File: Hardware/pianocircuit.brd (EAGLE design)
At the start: 160 x 82.2 mm, 64 parts, among them IC1 LM386M-1

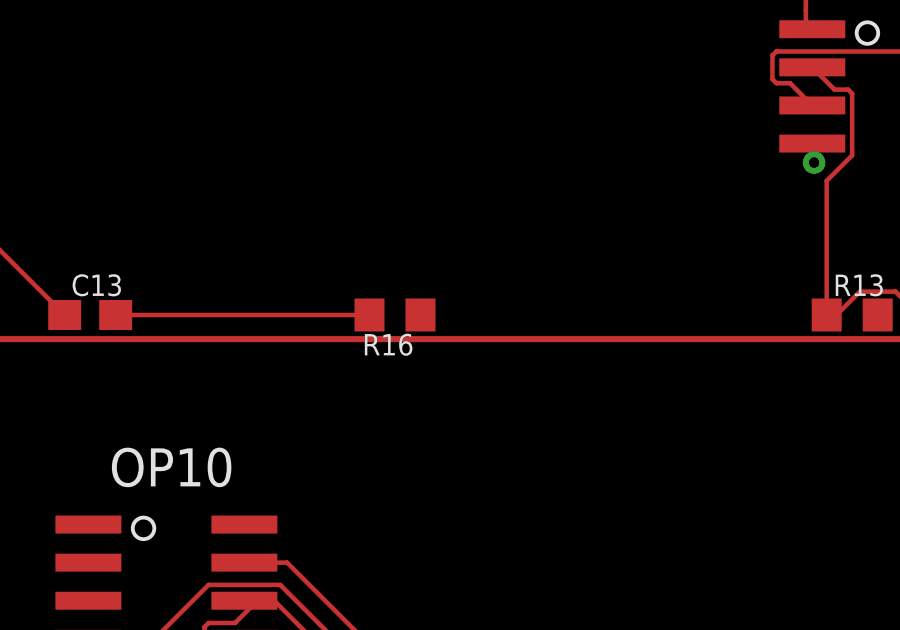
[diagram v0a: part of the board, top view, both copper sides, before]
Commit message: Routed Board and Updated Schematic
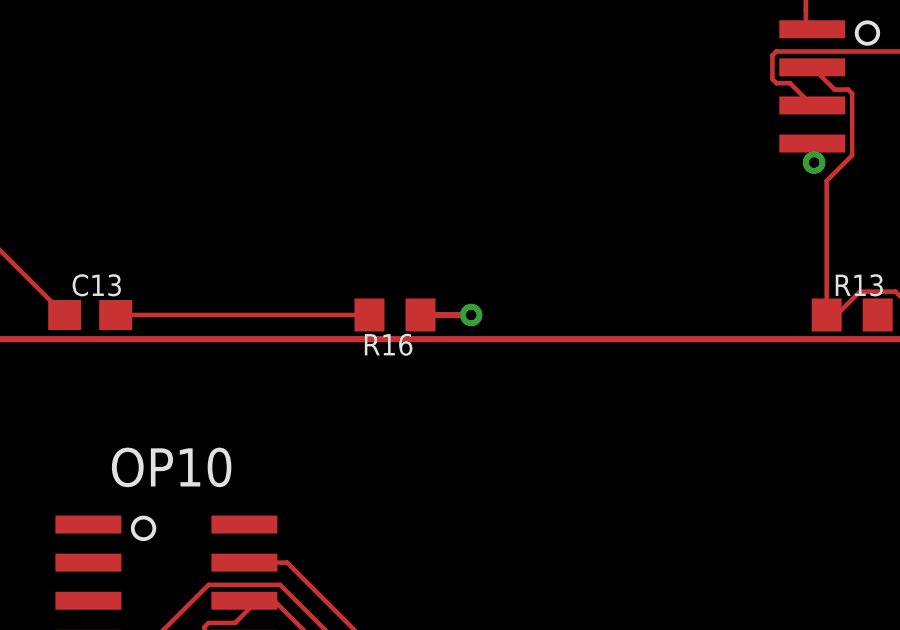
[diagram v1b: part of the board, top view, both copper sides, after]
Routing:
- net GND: track 28.0 -> 29.7 mm, vias 21 -> 22
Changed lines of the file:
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@@
 <wire x1="137.16" y1="38.735" x2="137.16" y2="38.1" width="0.2032" layer="1"/>
 <via x="137.16" y="38.1" extent="1-16" drill="0.35"/>
+<wire x1="38.95" y1="33.02" x2="40.64" y2="33.02" width="0.2032" layer="1"/>
+<via x="40.64" y="33.02" extent="1-16" drill="0.35"/>
 <wire x1="156.63" y1="16.51" x2="157.06" y2="19.05" width="0" layer="19" extent="1-1"/>
 <wire x1="154.94" y1="7.62" x2="156.63" y2="16.51" width="0" layer="19" extent="1-1"/>
-<wire x1="38.95" y1="33.02" x2="52.07" y2="38.1" width="0" layer="19" extent="1-1"/>
+<wire x1="138.43" y1="10.16" x2="153.25" y2="7.62" width="0" layer="19" extent="1-1"/>
+<wire x1="132.084075" y1="6.345925" x2="138.43" y2="10.16" width="0" layer="19" extent="1-1"/>
+<wire x1="123.61" y1="33.02" x2="138.37" y2="10.795" width="0" layer="19" extent="1-1"/>
+<wire x1="118.96" y1="33.02" x2="123.02256875" y2="34.12256875" width="0" layer="19" extent="1-1"/>
+<wire x1="106.68" y1="38.1" x2="118.96" y2="33.02" width="0" layer="19" extent="1-1"/>
+<wire x1="137.16" y1="38.1" x2="123.61" y2="33.02" width="0" layer="19" extent="1-1"/>
+<wire x1="107.95" y1="17.78" x2="119.38" y2="31.75" width="0" layer="19" extent="1-1"/>
+<wire x1="91.44" y1="12.7" x2="106.26" y2="17.78" width="0" layer="19" extent="1-1"/>
+<wire x1="83.82" y1="11.43" x2="91.44" y2="12.7" width="0" layer="19" extent="1-1"/>
+<wire x1="78.74" y1="13.12" x2="83.76" y2="12.065" width="0" layer="19" extent="1-1"/>
+<wire x1="64.77" y1="33.02" x2="77.47" y2="12.7" width="0" layer="19" extent="1-1"/>
+<wire x1="52.07" y1="38.1" x2="63.08" y2="33.02" width="0" layer="19" extent="1-1"/>
+<wire x1="40.64" y1="33.02" x2="52.07" y2="38.1" width="0" layer="19" extent="1-1"/>
+<wire x1="77.47" y1="38.1" x2="64.77" y2="33.02" width="0" layer="19" extent="1-1"/>
+<wire x1="27.88" y1="22.225" x2="38.95" y2="33.02" width="0" layer="19" extent="1-1"/>
+<wire x1="19.05" y1="15.24" x2="27.94" y2="21.59" width="0" layer="19" extent="1-1"/>
+<wire x1="16.51" y1="11.43" x2="19.47" y2="13.97" width="0" layer="19" extent="1-1"/>
+<wire x1="12.7" y1="6.35" x2="16.09" y2="10.16" width="0" layer="19" extent="1-1"/>
+<wire x1="20.32" y1="33.02" x2="27.88" y2="22.225" width="0" layer="19" extent="1-1"/>
+<wire x1="17.78" y1="54.61" x2="18.63" y2="33.02" width="0" layer="19" extent="1-1"/>
+<wire x1="16.57" y1="56.515" x2="16.57" y2="55.245" width="0" layer="19" extent="1-1"/>
 <wire x1="2.54" y1="52.07" x2="16.57" y2="55.245" width="0" layer="19" extent="1-1"/>
 </signal>

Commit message: Fixed Routing Errors
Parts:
- added R4: 3.3M, LinnesLab-Passives:R0603
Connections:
- new net N$12: R4.2
- net N$60: now also R4.1
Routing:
- net N$10: track 39.0 -> 91.5 mm
- net GND: track 29.7 -> 44.0 mm, vias 22 -> 24
- net N$60: track 14.3 -> 20.6 mm
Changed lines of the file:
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@@
 <attribute name="VALUE" x="4.52" y="64.625" size="1.27" layer="27"/>
+</element>
+<element name="R4" library="LinnesLab-Passives" package="R0603" package3d_urn="urn:adsk.eagle:package:15661944/2" value="3.3M" x="35.56" y="15.24" smashed="yes">
+<attribute name="NAME" x="34.925" y="15.875" size="0.7112" layer="25"/>
+<attribute name="VALUE" x="34.925" y="13.335" size="0.7112" layer="27"/>
 </element>
 </elements>
@@
 <wire x1="19.05" y1="13.97" x2="19.05" y2="15.24" width="0.2032" layer="1"/>
 <via x="19.05" y="15.24" extent="1-16" drill="0.35"/>
-<wire x1="16.57" y1="55.245" x2="17.78" y2="55.245" width="0.2032" layer="1"/>
-<wire x1="17.78" y1="55.245" x2="17.78" y2="54.8056" width="0.2032" layer="1"/>
-<wire x1="17.78" y1="54.8056" x2="17.78" y2="54.61" width="0.2032" layer="1"/>
-<via x="17.78" y="54.8056" extent="1-16" drill="0.35"/>
-<wire x1="16.57" y1="56.515" x2="16.57" y2="57.15" width="0.2032" layer="1"/>
-<wire x1="16.57" y1="57.15" x2="16.51" y2="57.15" width="0.2032" layer="1"/>
-<via x="16.51" y="57.15" extent="1-16" drill="0.35"/>
+<wire x1="16.57" y1="55.245" x2="19.05" y2="55.245" width="0.2032" layer="1"/>
+<wire x1="19.05" y1="55.245" x2="19.05" y2="54.8056" width="0.2032" layer="1"/>
+<wire x1="19.05" y1="54.8056" x2="19.05" y2="54.61" width="0.2032" layer="1"/>
+<via x="19.05" y="54.8056" extent="1-16" drill="0.35"/>
+<wire x1="16.57" y1="56.515" x2="16.57" y2="58.42" width="0.2032" layer="1"/>
+<wire x1="16.57" y1="58.42" x2="16.51" y2="58.42" width="0.2032" layer="1"/>
+<via x="16.51" y="58.42" extent="1-16" drill="0.35"/>
 <wire x1="18.63" y1="33.02" x2="20.32" y2="33.02" width="0.2032" layer="1"/>
 <via x="20.32" y="33.02" extent="1-16" drill="0.35"/>
@@
 <wire x1="91.44" y1="11.43" x2="91.44" y2="12.7" width="0.2032" layer="1"/>
 <via x="91.44" y="12.7" extent="1-16" drill="0.35"/>
-<wire x1="83.76" y1="12.065" x2="83.76" y2="11.43" width="0.2032" layer="1"/>
-<wire x1="83.76" y1="11.43" x2="83.82" y2="11.43" width="0.2032" layer="1"/>
-<via x="83.82" y="11.43" extent="1-16" drill="0.35"/>
+<wire x1="83.76" y1="12.065" x2="83.76" y2="10.16" width="0.2032" layer="1"/>
+<wire x1="83.76" y1="10.16" x2="83.82" y2="10.16" width="0.2032" layer="1"/>
+<via x="83.82" y="10.16" extent="1-16" drill="0.35"/>
 <wire x1="153.25" y1="7.62" x2="154.94" y2="7.62" width="0.2032" layer="1"/>
 <via x="154.94" y="7.62" extent="1-16" drill="0.35"/>
@@
 <contactref element="OP1" pad="4"/>
 <contactref element="OP10" pad="4"/>
-<wire x1="52.01" y1="38.735" x2="52.07" y2="38.735" width="0.2032" layer="1"/>
-<wire x1="52.07" y1="38.735" x2="52.07" y2="38.1" width="0.2032" layer="1"/>
-<via x="52.07" y="38.1" extent="1-16" drill="0.35"/>
+<wire x1="52.01" y1="38.735" x2="51.375" y2="38.1" width="0.2032" layer="1"/>
+<wire x1="51.375" y1="38.1" x2="49.53" y2="38.1" width="0.2032" layer="1"/>
+<via x="49.53" y="38.1" extent="1-16" drill="0.35"/>
 <wire x1="77.41" y1="38.735" x2="77.47" y2="38.735" width="0.2032" layer="1"/>
-<wire x1="77.47" y1="38.735" x2="77.47" y2="38.1" width="0.2032" layer="1"/>
-<via x="77.47" y="38.1" extent="1-16" drill="0.35"/>
+<wire x1="77.47" y1="38.735" x2="77.47" y2="36.83" width="0.2032" layer="1"/>
+<via x="77.47" y="36.83" extent="1-16" drill="0.35"/>
 <wire x1="27.88" y1="22.225" x2="27.94" y2="22.225" width="0.2032" layer="1"/>
 <wire x1="27.94" y1="22.225" x2="27.94" y2="21.59" width="0.2032" layer="1"/>
 <via x="27.94" y="21.59" extent="1-16" drill="0.35"/>
 <wire x1="106.62" y1="38.735" x2="106.68" y2="38.735" width="0.2032" layer="1"/>
-<wire x1="106.68" y1="38.735" x2="106.68" y2="38.1" width="0.2032" layer="1"/>
-<via x="106.68" y="38.1" extent="1-16" drill="0.35"/>
+<wire x1="106.68" y1="38.735" x2="106.68" y2="36.83" width="0.2032" layer="1"/>
+<via x="106.68" y="36.83" extent="1-16" drill="0.35"/>
 <wire x1="138.37" y1="10.795" x2="138.43" y2="10.795" width="0.2032" layer="1"/>
-<wire x1="138.43" y1="10.795" x2="138.43" y2="10.16" width="0.2032" layer="1"/>
-<via x="138.43" y="10.16" extent="1-16" drill="0.35"/>
+<wire x1="138.43" y1="10.795" x2="138.43" y2="8.89" width="0.2032" layer="1"/>
+<via x="138.43" y="8.89" extent="1-16" drill="0.35"/>
 <wire x1="137.1" y1="38.735" x2="137.16" y2="38.735" width="0.2032" layer="1"/>
-<wire x1="137.16" y1="38.735" x2="137.16" y2="38.1" width="0.2032" layer="1"/>
-<via x="137.16" y="38.1" extent="1-16" drill="0.35"/>
+<wire x1="137.16" y1="38.735" x2="137.16" y2="36.83" width="0.2032" layer="1"/>
+<via x="137.16" y="36.83" extent="1-16" drill="0.35"/>
 <wire x1="38.95" y1="33.02" x2="40.64" y2="33.02" width="0.2032" layer="1"/>
 <via x="40.64" y="33.02" extent="1-16" drill="0.35"/>
-<wire x1="156.63" y1="16.51" x2="157.06" y2="19.05" width="0" layer="19" extent="1-1"/>
-<wire x1="154.94" y1="7.62" x2="156.63" y2="16.51" width="0" layer="19" extent="1-1"/>
-<wire x1="138.43" y1="10.16" x2="153.25" y2="7.62" width="0" layer="19" extent="1-1"/>
-<wire x1="132.084075" y1="6.345925" x2="138.43" y2="10.16" width="0" layer="19" extent="1-1"/>
-<wire x1="123.61" y1="33.02" x2="138.37" y2="10.795" width="0" layer="19" extent="1-1"/>
-<wire x1="118.96" y1="33.02" x2="123.02256875" y2="34.12256875" width="0" layer="19" extent="1-1"/>
-<wire x1="106.68" y1="38.1" x2="118.96" y2="33.02" width="0" layer="19" extent="1-1"/>
-<wire x1="137.16" y1="38.1" x2="123.61" y2="33.02" width="0" layer="19" extent="1-1"/>
-<wire x1="107.95" y1="17.78" x2="119.38" y2="31.75" width="0" layer="19" extent="1-1"/>
-<wire x1="91.44" y1="12.7" x2="106.26" y2="17.78" width="0" layer="19" extent="1-1"/>
-<wire x1="83.82" y1="11.43" x2="91.44" y2="12.7" width="0" layer="19" extent="1-1"/>
-<wire x1="78.74" y1="13.12" x2="83.76" y2="12.065" width="0" layer="19" extent="1-1"/>
-<wire x1="64.77" y1="33.02" x2="77.47" y2="12.7" width="0" layer="19" extent="1-1"/>
-<wire x1="52.07" y1="38.1" x2="63.08" y2="33.02" width="0" layer="19" extent="1-1"/>
-<wire x1="40.64" y1="33.02" x2="52.07" y2="38.1" width="0" layer="19" extent="1-1"/>
-<wire x1="77.47" y1="38.1" x2="64.77" y2="33.02" width="0" layer="19" extent="1-1"/>
-<wire x1="27.88" y1="22.225" x2="38.95" y2="33.02" width="0" layer="19" extent="1-1"/>
-<wire x1="19.05" y1="15.24" x2="27.94" y2="21.59" width="0" layer="19" extent="1-1"/>
-<wire x1="16.51" y1="11.43" x2="19.47" y2="13.97" width="0" layer="19" extent="1-1"/>
-<wire x1="12.7" y1="6.35" x2="16.09" y2="10.16" width="0" layer="19" extent="1-1"/>
-<wire x1="20.32" y1="33.02" x2="27.88" y2="22.225" width="0" layer="19" extent="1-1"/>
-<wire x1="17.78" y1="54.61" x2="18.63" y2="33.02" width="0" layer="19" extent="1-1"/>
-<wire x1="16.57" y1="56.515" x2="16.57" y2="55.245" width="0" layer="19" extent="1-1"/>
-<wire x1="2.54" y1="52.07" x2="16.57" y2="55.245" width="0" layer="19" extent="1-1"/>
+<wire x1="156.63" y1="16.51" x2="154.94" y2="16.51" width="0.1524" layer="1"/>
+<via x="154.94" y="16.51" extent="1-16" drill="0.35"/>
+<wire x1="157.06" y1="19.05" x2="157.06" y2="19.47" width="0.1524" layer="1"/>
+<wire x1="157.06" y1="19.47" x2="156.21" y2="20.32" width="0.1524" layer="1"/>
+<via x="156.21" y="20.32" extent="1-16" drill="0.35"/>
+<wire x1="16.57" y1="55.245" x2="2.54" y2="52.07" width="0" layer="19" extent="1-1"/>
 </signal>
 <signal name="N$2">
@@
 <wire x1="134.62" y1="39.37" x2="135.255" y2="40.005" width="0.1524" layer="1"/>
 <wire x1="135.255" y1="40.005" x2="137.1" y2="40.005" width="0.1524" layer="1"/>
-<wire x1="129.96" y1="5.08" x2="158.33" y2="5.08" width="0" layer="19" extent="1-1"/>
+<wire x1="140.7146875" y1="18.5586" x2="139.5253125" y2="18.5586" width="0.1524" layer="1"/>
+<wire x1="139.5253125" y1="18.5586" x2="139.3914" y2="18.4246875" width="0.1524" layer="1"/>
+<wire x1="139.3914" y1="18.4246875" x2="139.3914" y2="17.1353125" width="0.1524" layer="1"/>
+<wire x1="158.33" y1="5.08" x2="158.0032875" y2="5.08" width="0.1524" layer="1"/>
+<wire x1="158.0032875" y1="5.08" x2="157.2246875" y2="4.3014" width="0.1524" layer="1"/>
+<wire x1="139.3914" y1="17.1353125" x2="139.6986" y2="16.8281125" width="0.1524" layer="1"/>
+<wire x1="139.6986" y1="16.8281125" x2="139.6986" y2="9.30045" width="0.1524" layer="1"/>
+<wire x1="139.6986" y1="9.30045" x2="138.32295" y2="7.9248" width="0.1524" layer="1"/>
+<wire x1="140.8986" y1="18.3746875" x2="140.7146875" y2="18.5586" width="0.1524" layer="1"/>
+<wire x1="138.32295" y1="7.9248" x2="132.8048" y2="7.9248" width="0.1524" layer="1"/>
+<wire x1="157.2246875" y1="4.3014" x2="143.7653125" y2="4.3014" width="0.1524" layer="1"/>
+<wire x1="143.7653125" y1="4.3014" x2="140.8986" y2="7.1681125" width="0.1524" layer="1"/>
+<wire x1="140.8986" y1="7.1681125" x2="140.8986" y2="18.3746875" width="0.1524" layer="1"/>
+<wire x1="132.8048" y1="7.9248" x2="129.96" y2="5.08" width="0.1524" layer="1"/>
 </signal>
 <signal name="N$11">
@@
 <wire x1="34.71" y1="8.89" x2="33.08" y2="10.52" width="0.1524" layer="1"/>
 <wire x1="33.08" y1="10.52" x2="33.08" y2="22.225" width="0.1524" layer="1"/>
+<contactref element="R4" pad="1"/>
+<wire x1="34.71" y1="8.89" x2="34.71" y2="15.24" width="0.1524" layer="1"/>
 </signal>
 <signal name="N$61">
@@
 <wire x1="2.54" y1="63.54" x2="7.62" y2="68.62" width="0.1524" layer="1"/>
 </signal>
+<signal name="N$12">
+<contactref element="R4" pad="2"/>
+</signal>
 </signals>

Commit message: board and schematic
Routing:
- net GND: track 44.0 -> 47.3 mm, vias 24 -> 25
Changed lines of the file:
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@@
 <wire x1="77.47" y1="38.735" x2="77.47" y2="36.83" width="0.2032" layer="1"/>
 <via x="77.47" y="36.83" extent="1-16" drill="0.35"/>
-<wire x1="27.88" y1="22.225" x2="27.94" y2="22.225" width="0.2032" layer="1"/>
-<wire x1="27.94" y1="22.225" x2="27.94" y2="21.59" width="0.2032" layer="1"/>
-<via x="27.94" y="21.59" extent="1-16" drill="0.35"/>
+<wire x1="27.88" y1="22.225" x2="27.245" y2="22.86" width="0.2032" layer="1"/>
+<wire x1="27.245" y1="22.86" x2="25.4" y2="22.86" width="0.2032" layer="1"/>
+<via x="25.4" y="22.86" extent="1-16" drill="0.35"/>
 <wire x1="106.62" y1="38.735" x2="106.68" y2="38.735" width="0.2032" layer="1"/>
 <wire x1="106.68" y1="38.735" x2="106.68" y2="36.83" width="0.2032" layer="1"/>
@@
 <wire x1="157.06" y1="19.47" x2="156.21" y2="20.32" width="0.1524" layer="1"/>
 <via x="156.21" y="20.32" extent="1-16" drill="0.35"/>
-<wire x1="16.57" y1="55.245" x2="2.54" y2="52.07" width="0" layer="19" extent="1-1"/>
+<wire x1="2.54" y1="52.07" x2="3.81" y2="52.07" width="0.1524" layer="1"/>
+<via x="3.81" y="52.07" extent="1-16" drill="0.35"/>
 </signal>
 <signal name="N$2">

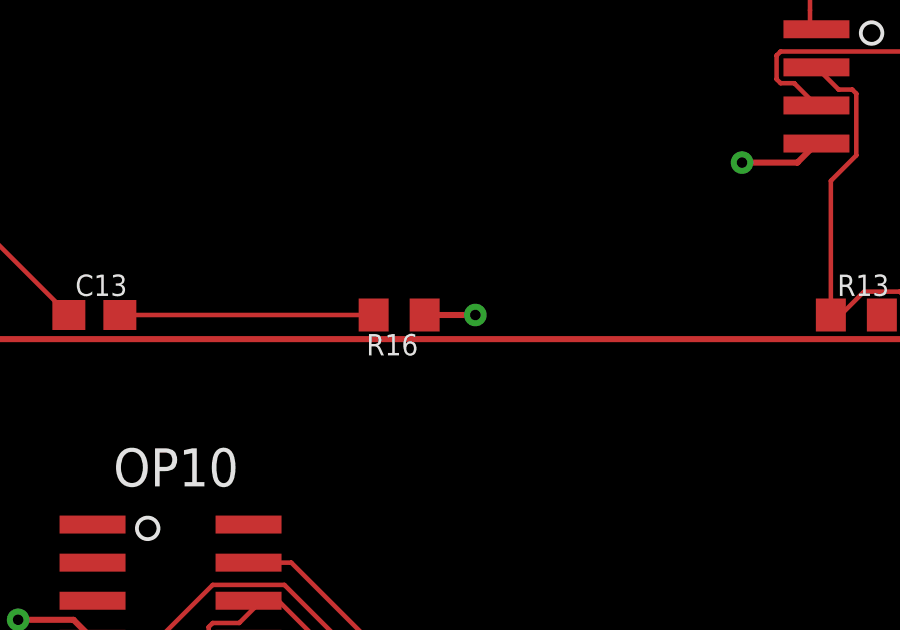
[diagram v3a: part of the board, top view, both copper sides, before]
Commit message: Fixed inconsistent board and schematic
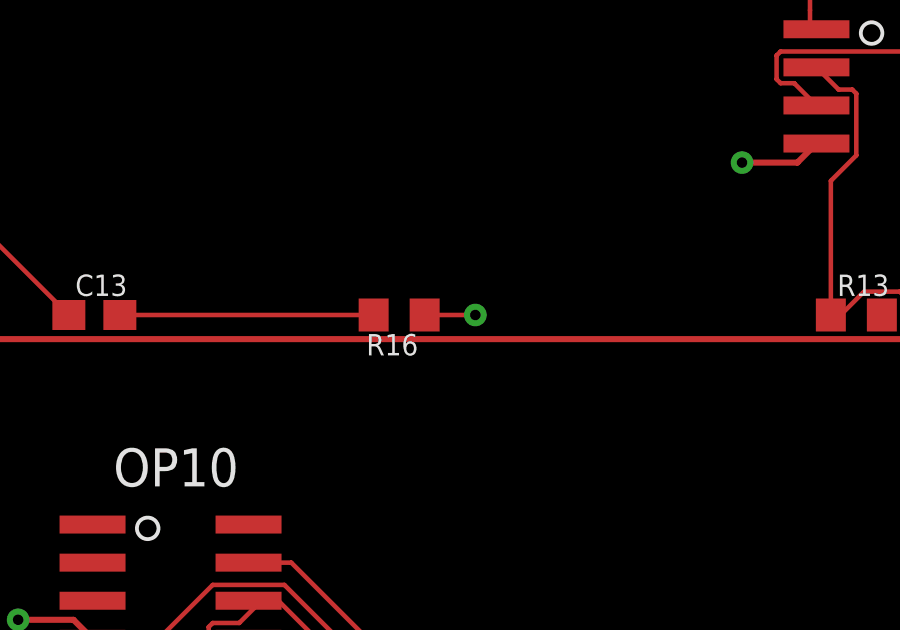
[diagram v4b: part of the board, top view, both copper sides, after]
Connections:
- net 5V renamed V+
- net GND renamed V-
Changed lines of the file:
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@@
 </elements>
 <signals>
-<signal name="GND">
+<signal name="V-">
 <contactref element="R30" pad="1"/>
 <contactref element="OP6" pad="4"/>
@@
 <wire x1="137.16" y1="38.735" x2="137.16" y2="36.83" width="0.2032" layer="1"/>
 <via x="137.16" y="36.83" extent="1-16" drill="0.35"/>
-<wire x1="38.95" y1="33.02" x2="40.64" y2="33.02" width="0.2032" layer="1"/>
-<via x="40.64" y="33.02" extent="1-16" drill="0.35"/>
 <wire x1="156.63" y1="16.51" x2="154.94" y2="16.51" width="0.1524" layer="1"/>
 <via x="154.94" y="16.51" extent="1-16" drill="0.35"/>
@@
 <wire x1="2.54" y1="52.07" x2="3.81" y2="52.07" width="0.1524" layer="1"/>
 <via x="3.81" y="52.07" extent="1-16" drill="0.35"/>
+<wire x1="38.95" y1="33.02" x2="40.64" y2="33.02" width="0.1524" layer="1"/>
+<via x="40.64" y="33.02" extent="1-16" drill="0.35"/>
 </signal>
 <signal name="N$2">
@@
 <wire x1="91.02" y1="16.2117125" x2="90.1546875" y2="15.3464" width="0.1524" layer="1"/>
 </signal>
-<signal name="5V">
+<signal name="V+">
 <contactref element="OP11" pad="8"/>
 <contactref element="OP2" pad="8"/>
